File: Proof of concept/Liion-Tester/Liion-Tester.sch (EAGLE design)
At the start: 22 parts, among them Q1 BC327, Q2 SI4403DDY-T1-GE3, U1 1042, U2 NCP1854FCCT1G, U3 BQ27427YZFR

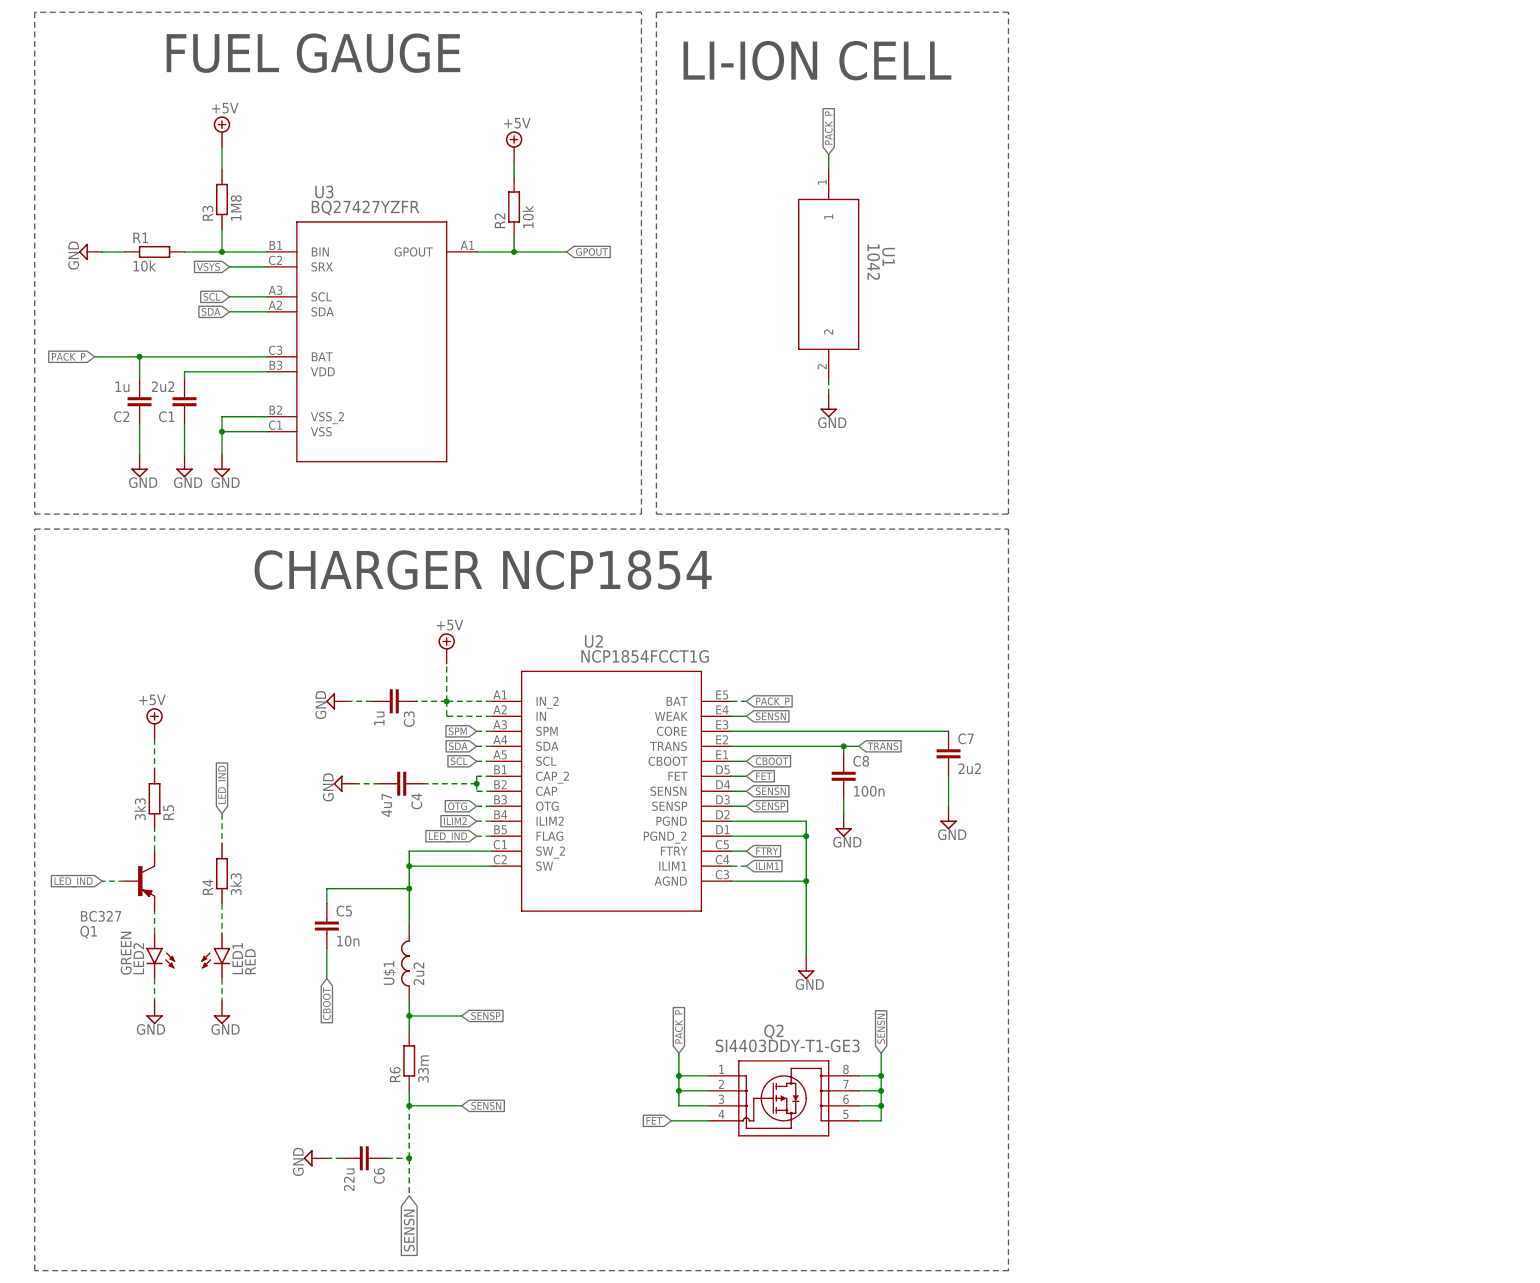
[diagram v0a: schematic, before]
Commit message: Rework of BQ and NCP. Connector added to schematic.
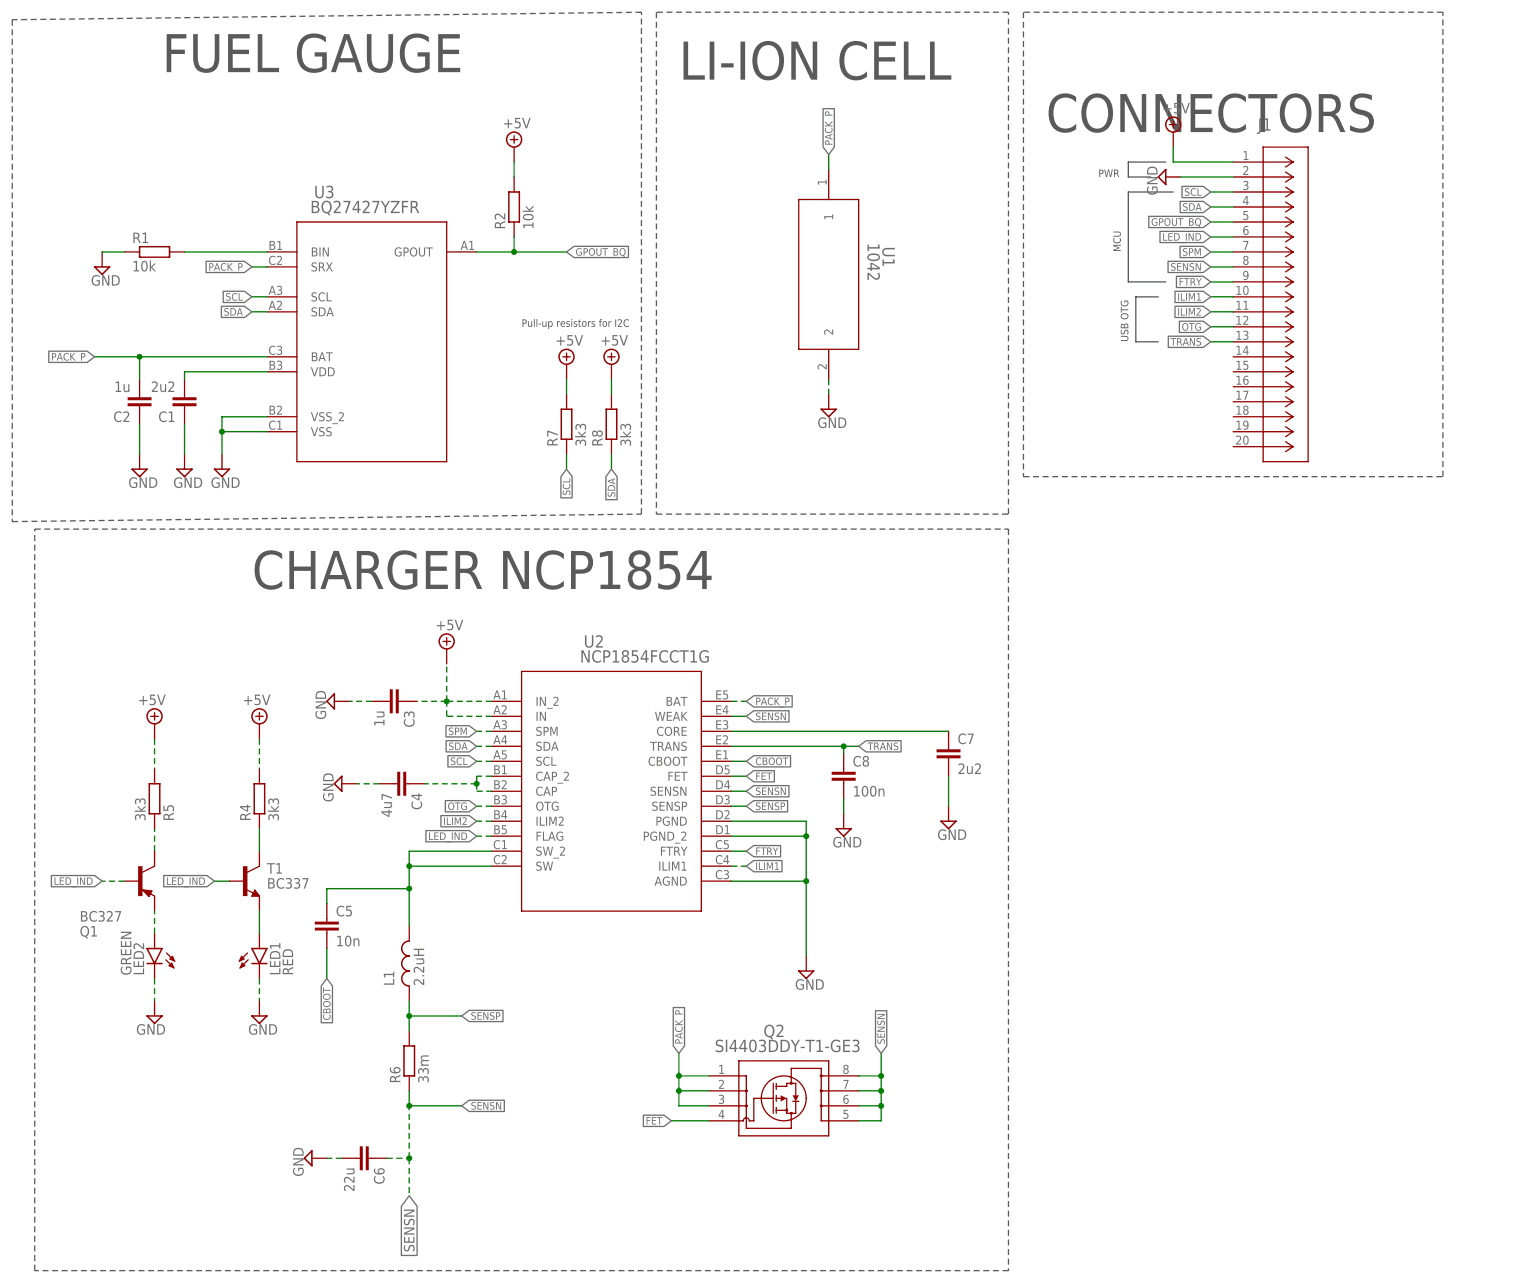
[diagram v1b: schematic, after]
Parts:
- removed R3: 1M8, rcl:R-EU_R0603
- added J1: 250-120, custom_library:250-120
- added R7, R8: 3k3, rcl:R-EU_R0603
- added T1: BC337, transistor:BC337
- L1: value 2u2 -> 2.2uH
- renumbered U$1 to L1
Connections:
- removed net GPOUT: R2.1, U3.GPOUT
- removed net VSYS: U3.SRX
- new net GPOUT_BQ: J1.5, R2.1, U3.GPOUT
- new net N$9: LED1.A, T1.E
- net +5V: now also J1.1, R4.2, R7.2, R8.2; no longer R3.2
- net FTRY: now also J1.9
- net GND: now also J1.2
- net ILIM1: now also J1.10
- net ILIM2: now also J1.11
- net LED_IND: now also J1.6, T1.B; no longer R4.2
- net N$2: no longer R3.1
- net N$4: now also T1.C; no longer LED1.A
- net OTG: now also J1.12
- net PACK_P: now also U3.SRX
- net SCL: now also J1.3, R7.1
- net SDA: now also J1.4, R8.1
- net SENSN: now also J1.8
- net SPM: now also J1.7
- net TRANS: now also J1.13
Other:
- note added: "CONNECTORS"
- note added: "MCU"
- note added: "PWR"
- note added: "Pull-up resistors for I2C"
- note added: "USB OTG"
- moved on the sheet: LED1, R4

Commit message: Final changes in .sch before making .brd
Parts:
- removed J1: 250-120, custom_library:250-120
- removed LED1: RED, led:LED
- removed Q1: BC327, transistor-pnp:BC327
- removed R4: 3k3, rcl:R-EU_R0603
- removed T1: BC337, transistor:BC337
- added JUMPERS: (no value), pinhead:PINHD-2X2
- added MCU: 250-109, custom_library:250-109
- added POWER, USB: 250-102, custom_library:250-102
- R7, R8: value 3k3 -> 3k3-DNP
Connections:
- removed net N$4: R4.1, T1.C
- removed net N$6: Q1.C, R5.1
- removed net N$9: LED1.A, T1.E
- new net BAT_NCP: JUMPERS.3, U2.BAT
- new net SRX_BQ: JUMPERS.1, U3.SRX
- net +5V: now also POWER.1; no longer J1.1, R4.2, R5.2
- net FTRY: now also MCU.7; no longer J1.9
- net GND: now also POWER.2; no longer J1.2, LED1.C
- net GPOUT_BQ: now also MCU.3; no longer J1.5
- net ILIM1: now also MCU.8; no longer J1.10
- net ILIM2: now also MCU.9; no longer J1.11
- net LED_IND: now also MCU.4, R5.2; no longer J1.6, Q1.B, T1.B
- net N$5: now also R5.1; no longer Q1.E
- net OTG: now also USB.1; no longer J1.12
- net PACK_P: now also JUMPERS.2, JUMPERS.4; no longer U2.BAT, U3.SRX
- net SCL: now also MCU.1; no longer J1.3
- net SDA: now also MCU.2; no longer J1.4
- net SENSN: now also MCU.6; no longer J1.8
- net SPM: now also MCU.5; no longer J1.7
- net TRANS: now also USB.2; no longer J1.13
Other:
- note added: "Default: 1&3 connected, 2&4 floating Fuel gauge disconnected: 1&2 connected, 3&4 connected"
- note added: "JUMPERS"
- moved on the sheet: LED2, R5

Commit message: Version control
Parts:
- R7, R8: value 3k3-DNP -> DNP-3k3
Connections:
- net BAT_NCP: now also JUMPERS.1; no longer JUMPERS.3
- net SRX_BQ: now also JUMPERS.3; no longer JUMPERS.1
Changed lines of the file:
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@@
 <setting verticaltext="up"/>
 </settings>
-<grid distance="0.05" unitdist="inch" unit="inch" style="lines" multiple="1" display="yes" altdistance="0.01" altunitdist="inch" altunit="inch"/>
+<grid distance="0.1" unitdist="inch" unit="inch" style="lines" multiple="1" display="no" altdistance="0.01" altunitdist="inch" altunit="inch"/>
 <layers>
 <layer number="1" name="Top" color="4" fill="1" visible="no" active="no"/>
@@
 <part name="SUPPLY18" library="supply2" library_urn="urn:adsk.eagle:library:372" deviceset="+5V" device=""/>
 <part name="SUPPLY19" library="supply2" library_urn="urn:adsk.eagle:library:372" deviceset="+5V" device=""/>
-<part name="R7" library="rcl" library_urn="urn:adsk.eagle:library:334" deviceset="R-EU_" device="R0603" package3d_urn="urn:adsk.eagle:package:23555/3" value="3k3-DNP"/>
-<part name="R8" library="rcl" library_urn="urn:adsk.eagle:library:334" deviceset="R-EU_" device="R0603" package3d_urn="urn:adsk.eagle:package:23555/3" value="3k3-DNP"/>
+<part name="R7" library="rcl" library_urn="urn:adsk.eagle:library:334" deviceset="R-EU_" device="R0603" package3d_urn="urn:adsk.eagle:package:23555/3" value="DNP-3k3"/>
+<part name="R8" library="rcl" library_urn="urn:adsk.eagle:library:334" deviceset="R-EU_" device="R0603" package3d_urn="urn:adsk.eagle:package:23555/3" value="DNP-3k3"/>
 <part name="SUPPLY20" library="supply2" library_urn="urn:adsk.eagle:library:372" deviceset="GND" device=""/>
 <part name="SUPPLY21" library="supply2" library_urn="urn:adsk.eagle:library:372" deviceset="+5V" device=""/>
@@
 </segment>
 <segment>
+<pinref part="JUMPERS" gate="A" pin="1"/>
+<wire x1="97.79" y1="-54.61" x2="88.9" y2="-54.61" width="0.1524" layer="91"/>
+<label x="88.9" y="-54.61" size="1.27" layer="95" rot="R180" xref="yes"/>
+</segment>
+</net>
+<net name="SRX_BQ" class="0">
+<segment>
+<pinref part="U3" gate="A" pin="SRX"/>
+<wire x1="-57.15" y1="15.24" x2="-59.69" y2="15.24" width="0.1524" layer="91"/>
+<label x="-59.69" y="15.24" size="1.27" layer="95" rot="R180" xref="yes"/>
+</segment>
+<segment>
 <pinref part="JUMPERS" gate="A" pin="3"/>
 <wire x1="97.79" y1="-57.15" x2="88.9" y2="-57.15" width="0.1524" layer="91"/>
@@
 </segment>
 </net>
-<net name="SRX_BQ" class="0">
-<segment>
-<pinref part="JUMPERS" gate="A" pin="1"/>
-<wire x1="97.79" y1="-54.61" x2="88.9" y2="-54.61" width="0.1524" layer="91"/>
-<label x="88.9" y="-54.61" size="1.27" layer="95" rot="R180" xref="yes"/>
-</segment>
-<segment>
-<pinref part="U3" gate="A" pin="SRX"/>
-<wire x1="-57.15" y1="15.24" x2="-59.69" y2="15.24" width="0.1524" layer="91"/>
-<label x="-59.69" y="15.24" size="1.27" layer="95" rot="R180" xref="yes"/>
-</segment>
-</net>

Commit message: Finished .brd with changes in schematic
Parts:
- removed LED2: GREEN, led:LED
- added LED1: FYLS-1206PGC, custom_library:QBLP650-IW
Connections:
- removed net N$5: LED2.A, R5.1
- new net N$4: LED1.ANODE, R5.1
- net FTRY: now also MCU.6; no longer MCU.7
- net GND: now also LED1.CATHODE; no longer LED2.C
- net GPOUT_BQ: now also MCU.5; no longer MCU.3
- net ILIM2: now also MCU.7; no longer MCU.9
- net OTG: now also USB.2; no longer USB.1
- net SCL: now also MCU.3; no longer MCU.1
- net SENSN: now also MCU.9; no longer MCU.6
- net SPM: now also MCU.1; no longer MCU.5
- net TRANS: now also USB.1; no longer USB.2
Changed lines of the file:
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@@
 <part name="C4" library="rcl" library_urn="urn:adsk.eagle:library:334" deviceset="C-EU" device="C0603" package3d_urn="urn:adsk.eagle:package:23616/2" value="4u7"/>
 <part name="SUPPLY10" library="supply2" library_urn="urn:adsk.eagle:library:372" deviceset="GND" device=""/>
-<part name="LED2" library="led" library_urn="urn:adsk.eagle:library:259" deviceset="LED" device="" package3d_urn="urn:adsk.eagle:package:15825/1" value="GREEN"/>
 <part name="R5" library="rcl" library_urn="urn:adsk.eagle:library:334" deviceset="R-EU_" device="R0603" package3d_urn="urn:adsk.eagle:package:23555/3" value="3k3"/>
 <part name="SUPPLY13" library="supply2" library_urn="urn:adsk.eagle:library:372" deviceset="GND" device=""/>
@@
 <part name="MCU" library="custom_library" deviceset="250-109" device=""/>
 <part name="JUMPERS" library="pinhead" library_urn="urn:adsk.eagle:library:325" deviceset="PINHD-2X2" device="" package3d_urn="urn:adsk.eagle:package:22455/2"/>
+<part name="LED1" library="custom_library" deviceset="QBLP650-IW" device="" value="FYLS-1206PGC"/>
 </parts>
 <sheets>
@@
 <attribute name="VALUE" x="-47.625" y="-70.485" size="1.778" layer="96" rot="R270"/>
 </instance>
-<instance part="LED2" gate="G$1" x="-58.42" y="-102.87" smashed="yes" rot="MR0">
-<attribute name="NAME" x="-61.976" y="-107.442" size="1.778" layer="95" rot="MR90"/>
-<attribute name="VALUE" x="-64.135" y="-107.442" size="1.778" layer="96" rot="MR90"/>
-</instance>
 <instance part="R5" gate="G$1" x="-58.42" y="-87.63" smashed="yes" rot="MR90">
 <attribute name="NAME" x="-56.9214" y="-91.44" size="1.778" layer="95" rot="MR90"/>
 <attribute name="VALUE" x="-61.722" y="-91.44" size="1.778" layer="96" rot="MR90"/>
 </instance>
-<instance part="SUPPLY13" gate="GND" x="-58.42" y="-114.3" smashed="yes" rot="MR0">
-<attribute name="VALUE" x="-56.515" y="-117.475" size="1.778" layer="96" rot="MR0"/>
+<instance part="SUPPLY13" gate="GND" x="-58.42" y="-118.11" smashed="yes" rot="MR0">
+<attribute name="VALUE" x="-56.515" y="-121.285" size="1.778" layer="96" rot="MR0"/>
 </instance>
 <instance part="R6" gate="G$1" x="-33.02" y="-119.38" smashed="yes" rot="R90">
@@
 <attribute name="NAME" x="93.98" y="-51.435" size="1.778" layer="95"/>
 <attribute name="VALUE" x="93.98" y="-62.23" size="1.778" layer="96"/>
+</instance>
+<instance part="LED1" gate="A" x="-58.42" y="-101.6" smashed="yes" rot="R270">
+<attribute name="VALUE" x="-66.4972" y="-88.8238" size="3.4798" layer="96" ratio="10" rot="SR270"/>
+<attribute name="NAME" x="-55.7276" y="-101.3206" size="3.4798" layer="95" ratio="10" rot="SR270"/>
 </instance>
 </instances>
@@
 <wire x1="-38.1" y1="-72.39" x2="-41.91" y2="-72.39" width="0.1524" layer="91" style="longdash"/>
 <pinref part="SUPPLY10" gate="GND" pin="GND"/>
-</segment>
-<segment>
-<pinref part="LED2" gate="G$1" pin="C"/>
-<pinref part="SUPPLY13" gate="GND" pin="GND"/>
-<wire x1="-58.42" y1="-107.95" x2="-58.42" y2="-111.76" width="0.1524" layer="91" style="longdash"/>
 </segment>
 <segment>
@@
 <pinref part="POWER" gate="A" pin="2"/>
 </segment>
+<segment>
+<pinref part="LED1" gate="A" pin="CATHODE"/>
+<pinref part="SUPPLY13" gate="GND" pin="GND"/>
+<wire x1="-58.42" y1="-111.76" x2="-58.42" y2="-115.57" width="0.1524" layer="91"/>
+</segment>
 </net>
 <net name="N$1" class="0">
@@
 </segment>
 <segment>
-<wire x1="109.22" y1="22.86" x2="102.87" y2="22.86" width="0.1524" layer="91"/>
-<label x="102.87" y="22.86" size="1.27" layer="95" rot="R180" xref="yes"/>
-<pinref part="MCU" gate="A" pin="1"/>
+<wire x1="109.22" y1="17.78" x2="102.87" y2="17.78" width="0.1524" layer="91"/>
+<label x="102.87" y="17.78" size="1.27" layer="95" rot="R180" xref="yes"/>
+<pinref part="MCU" gate="A" pin="3"/>
 </segment>
 </net>
@@
 </segment>
 <segment>
-<wire x1="109.22" y1="17.78" x2="102.87" y2="17.78" width="0.1524" layer="91"/>
-<label x="102.87" y="17.78" size="1.27" layer="95" rot="R180" xref="yes"/>
-<pinref part="MCU" gate="A" pin="3"/>
+<wire x1="109.22" y1="12.7" x2="102.87" y2="12.7" width="0.1524" layer="91"/>
+<label x="102.87" y="12.7" size="1.27" layer="95" rot="R180" xref="yes"/>
+<pinref part="MCU" gate="A" pin="5"/>
 </segment>
 </net>
@@
 </segment>
 <segment>
-<wire x1="109.22" y1="12.7" x2="102.87" y2="12.7" width="0.1524" layer="91"/>
-<label x="102.87" y="12.7" size="1.27" layer="95" rot="R180" xref="yes"/>
-<pinref part="MCU" gate="A" pin="5"/>
+<wire x1="109.22" y1="22.86" x2="102.87" y2="22.86" width="0.1524" layer="91"/>
+<label x="102.87" y="22.86" size="1.27" layer="95" rot="R180" xref="yes"/>
+<pinref part="MCU" gate="A" pin="1"/>
 </segment>
 </net>
@@
 </segment>
 <segment>
-<wire x1="109.22" y1="-7.62" x2="102.87" y2="-7.62" width="0.1524" layer="91"/>
-<label x="102.87" y="-7.62" size="1.27" layer="95" rot="R180" xref="yes"/>
-<pinref part="USB" gate="A" pin="1"/>
+<wire x1="109.22" y1="-10.16" x2="102.87" y2="-10.16" width="0.1524" layer="91"/>
+<label x="102.87" y="-10.16" size="1.27" layer="95" rot="R180" xref="yes"/>
+<pinref part="USB" gate="A" pin="2"/>
 </segment>
 </net>
@@
 </segment>
 <segment>
-<wire x1="109.22" y1="2.54" x2="102.87" y2="2.54" width="0.1524" layer="91"/>
-<label x="102.87" y="2.54" size="1.27" layer="95" rot="R180" xref="yes"/>
-<pinref part="MCU" gate="A" pin="9"/>
+<wire x1="109.22" y1="7.62" x2="102.87" y2="7.62" width="0.1524" layer="91"/>
+<label x="102.87" y="7.62" size="1.27" layer="95" rot="R180" xref="yes"/>
+<pinref part="MCU" gate="A" pin="7"/>
 </segment>
 </net>
@@
 <label x="102.87" y="15.24" size="1.27" layer="95" rot="R180" xref="yes"/>
 <pinref part="MCU" gate="A" pin="4"/>
-</segment>
-</net>
-<net name="N$5" class="0">
-<segment>
-<pinref part="LED2" gate="G$1" pin="A"/>
-<wire x1="-58.42" y1="-100.33" x2="-58.42" y2="-92.71" width="0.1524" layer="91" style="longdash"/>
-<pinref part="R5" gate="G$1" pin="1"/>
 </segment>
 </net>
@@
 </segment>
 <segment>
-<wire x1="109.22" y1="10.16" x2="102.87" y2="10.16" width="0.1524" layer="91"/>
-<label x="102.87" y="10.16" size="1.27" layer="95" rot="R180" xref="yes"/>
-<pinref part="MCU" gate="A" pin="6"/>
+<wire x1="109.22" y1="2.54" x2="102.87" y2="2.54" width="0.1524" layer="91"/>
+<label x="102.87" y="2.54" size="1.27" layer="95" rot="R180" xref="yes"/>
+<pinref part="MCU" gate="A" pin="9"/>
 </segment>
 </net>
@@
 </segment>
 <segment>
-<wire x1="109.22" y1="-10.16" x2="102.87" y2="-10.16" width="0.1524" layer="91"/>
-<label x="102.87" y="-10.16" size="1.27" layer="95" rot="R180" xref="yes"/>
-<pinref part="USB" gate="A" pin="2"/>
+<wire x1="109.22" y1="-7.62" x2="102.87" y2="-7.62" width="0.1524" layer="91"/>
+<label x="102.87" y="-7.62" size="1.27" layer="95" rot="R180" xref="yes"/>
+<pinref part="USB" gate="A" pin="1"/>
 </segment>
 </net>
@@
 </segment>
 <segment>
-<wire x1="109.22" y1="7.62" x2="102.87" y2="7.62" width="0.1524" layer="91"/>
-<label x="102.87" y="7.62" size="1.27" layer="95" rot="R180" xref="yes"/>
-<pinref part="MCU" gate="A" pin="7"/>
+<wire x1="109.22" y1="10.16" x2="102.87" y2="10.16" width="0.1524" layer="91"/>
+<label x="102.87" y="10.16" size="1.27" layer="95" rot="R180" xref="yes"/>
+<pinref part="MCU" gate="A" pin="6"/>
 </segment>
 </net>
@@
 </segment>
 </net>
+<net name="N$4" class="0">
+<segment>
+<pinref part="R5" gate="G$1" pin="1"/>
+<pinref part="LED1" gate="A" pin="ANODE"/>
+<wire x1="-58.42" y1="-92.71" x2="-58.42" y2="-101.6" width="0.1524" layer="91"/>
+</segment>
+</net>
